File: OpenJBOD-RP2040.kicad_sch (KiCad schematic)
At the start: 61 parts, among them J1 ATX-24, J2 Bus_PCI_Express_x1, J3 Conn_02x02_Counter_Clockwise, J4 UART, J5 USB_C_Receptacle_USB2.0_16P, J9 TEMP1, Q1 MMBT3904, Q2 MMBT3904, SW1 TC-6615-6-260G, SW2 TC-6615-6-260G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

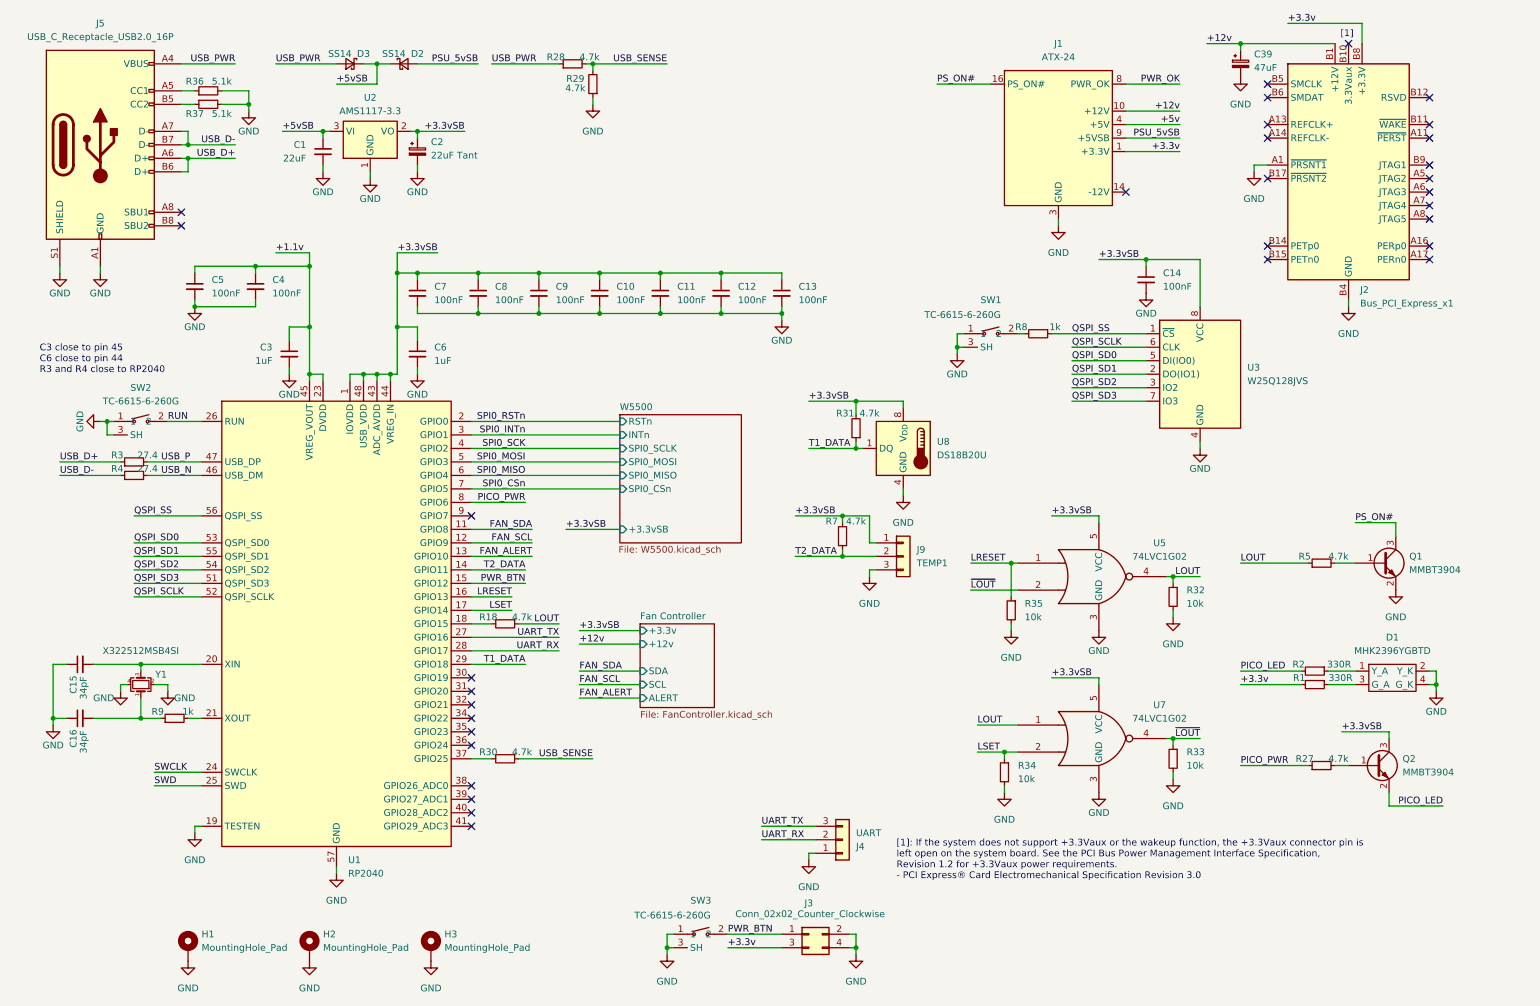
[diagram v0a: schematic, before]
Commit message: sch/pcb: SR latch caps
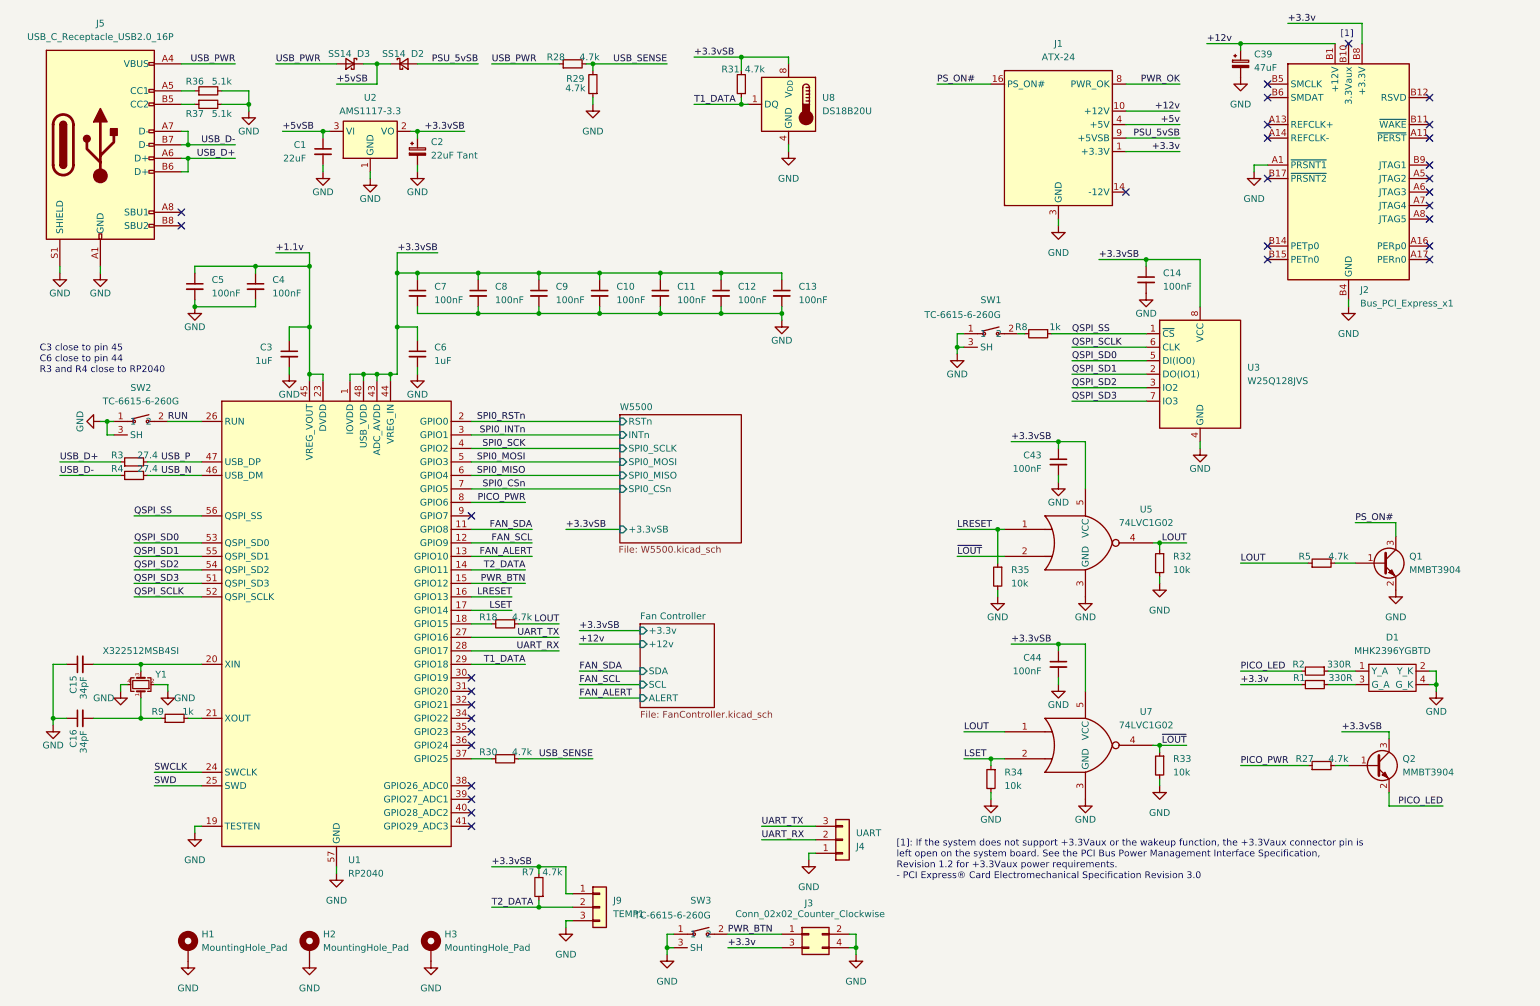
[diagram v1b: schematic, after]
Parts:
- added C43, C44: 100nF, Capacitor_SMD:C_0402_1005Metric, symbol Device:C_Small
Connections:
- net +3.3vSB: now also C43.1, C44.1
- net GND: now also C43.2, C44.2
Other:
- moved on the sheet: J9, R31, R32, R33, R34, R35, R7, U5, U7, U8

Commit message: schematic cleanup
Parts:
- removed C1: 22uF, Capacitor_SMD:C_1206_3216Metric, symbol Device:C_Small
- removed C10, C11, C12, C13, C14, C4, C43, C44, C5, C7, C8, C9: 100nF, Capacitor_SMD:C_0402_1005Metric, symbol Device:C_Small
- removed C15, C16: 34pF, Capacitor_SMD:C_0603_1608Metric, symbol Device:C_Small
- removed C2: 22uF Tant, Capacitor_Tantalum_SMD:CP_EIA-3216-18_Kemet-A, symbol Device:C_Polarized_Small
- removed C3, C6: 1uF, Capacitor_SMD:C_0402_1005Metric, symbol Device:C_Small
- removed D2, D3: SS14, Diode_SMD:D_SMA, symbol Device:D_Schottky_Small
- removed J1: ATX-24, OpenJBOD_Library:CONN-TH_M4202V-2X12P, symbol Connector:ATX-24
- removed J5: USB_C_Receptacle_USB2.0_16P, OpenJBOD_Library:USB-C-SMD_TYPE-C16PIN, symbol Connector:USB_C_Receptacle_USB2.0_16P
- removed J9: TEMP1, Connector_PinHeader_2.54mm:PinHeader_1x03_P2.54mm_Vertical, symbol Connector_Generic:Conn_01x03
- removed Q1: MMBT3904, Package_TO_SOT_SMD:SOT-23, symbol Transistor_BJT:MMBT3904
- removed R18, R28, R29, R30, R31, R5, R7: 4.7k, Resistor_SMD:R_0402_1005Metric, symbol Device:R_Small
- removed R3, R4: 27.4, Resistor_SMD:R_0402_1005Metric, symbol Device:R_Small
- removed R32, R33, R34, R35: 10k, Capacitor_SMD:C_0402_1005Metric, symbol Device:R_Small
- removed R36, R37: 5.1k, Capacitor_SMD:C_0402_1005Metric, symbol Device:R_Small
- removed R8, R9: 1k, Resistor_SMD:R_0402_1005Metric, symbol Device:R_Small
- removed SW1, SW2: TC-6615-6-260G, OpenJBOD_Library:KEY-TH_TC-6615-6-160G, symbol OpenJBOD:TC-6615-6-260G
- removed U1: RP2040, Package_DFN_QFN:QFN-56-1EP_7x7mm_P0.4mm_EP3.2x3.2mm, symbol MCU_RaspberryPi:RP2040
- removed U2: AMS1117-3.3, Package_TO_SOT_SMD:SOT-223-3_TabPin2, symbol Regulator_Linear:AMS1117-3.3
- removed U3: W25Q128JVS, Package_SO:SOIC-8_5.23x5.23mm_P1.27mm, symbol Memory_Flash:W25Q128JVS
- removed U5, U7: 74LVC1G02, Package_TO_SOT_SMD:SOT-353_SC-70-5, symbol 74xGxx:74LVC1G02
- removed U8: DS18B20U, Package_SO:MSOP-8_3x3mm_P0.65mm, symbol Sensor_Temperature:DS18B20U
- removed Y1: X322512MSB4SI, Crystal:Crystal_SMD_3225-4Pin_3.2x2.5mm, symbol Device:Crystal_GND24_Small
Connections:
- no-connect marks 32 -> 18
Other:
- sheet Fan Controller renamed Environment
- added sheet MCU (MCU.kicad_sch)
- added sheet Power (Power.kicad_sch)
- sheet Environment: file FanController.kicad_sch -> Environment.kicad_sch
- sheet Environment ports: added T1_DATA, T2_DATA; removed none
- note added: "EMC2301 DS18B20"
- note added: "Front Panel IO"
- note added: "LED Indicators"
- note added: "Mounting Holes"
- note added: "PCIe x1 Header"
- note added: "RP2040 QSPI Flash GPIO BOOTSEL switch RESET switch"
- note added: "UART"
- note added: "USB-C 24p ATX SR Latch USB Sensing 3.3v Standby"
- note added: "W5500 RJ45 NIC"
- note removed: "C3 close to pin 45 C6 close to pin 44 R3 and R4 close to RP2040"
- moved on the sheet: C39, D1, H1, H2, H3, J2, J3, J4, Q2, R1, R2, R27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

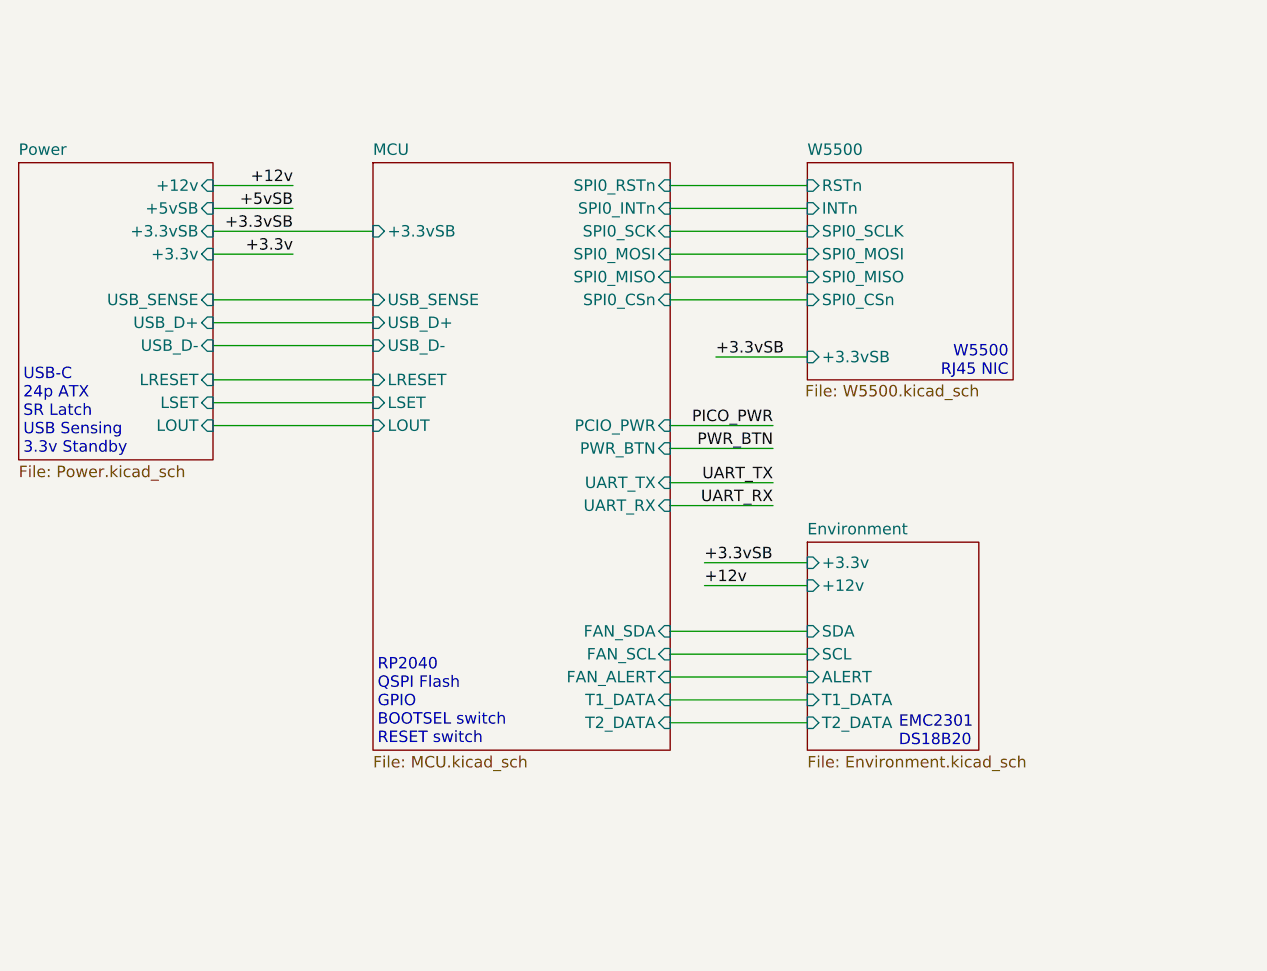
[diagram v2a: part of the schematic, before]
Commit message: rev5
Added MACROM (specific ROM holding MAC address and (optionally) board
revision)
Added more circuitry to protect the EMC2301, allowing for use with fans
with internal pull-ups.
Added USB-C
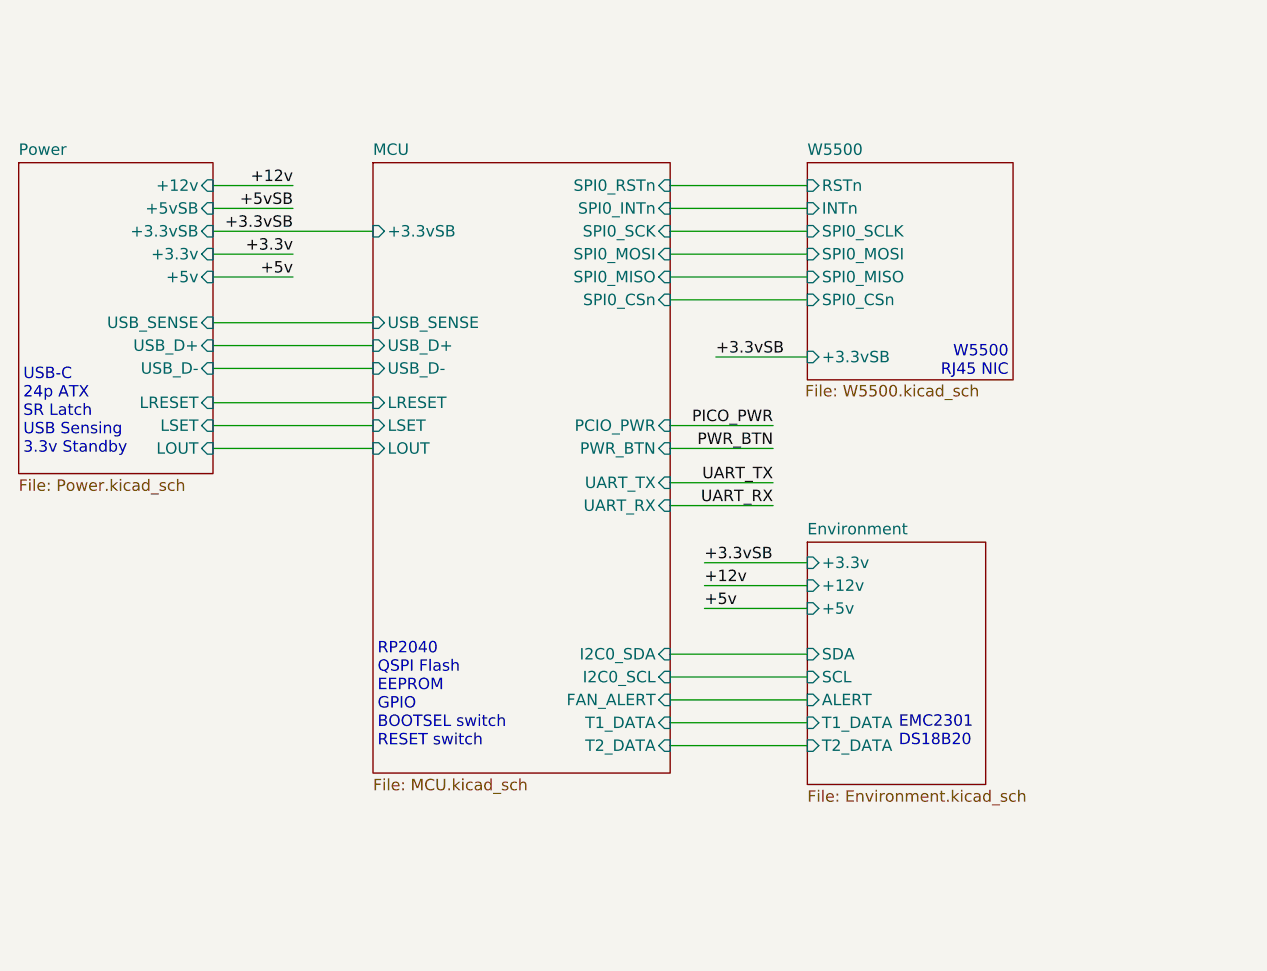
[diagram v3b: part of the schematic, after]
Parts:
- C39: JLCPCB_PN C2836440 -> (none); LCSC Part # (none) -> C2836440
- D1: JLCPCB_PN C2764899 -> (none); LCSC Part # (none) -> C2764899
- J2: JLCPCB_PN C5210918 -> (none); LCSC Part # (none) -> C5210918
- J3: JLCPCB_PN C492419 -> (none); LCSC Part # (none) -> C492419
- J4: JLCPCB_PN C2894945 -> (none); LCSC Part # (none) -> C2894945
- Q2: JLCPCB_PN C20526 -> (none); LCSC Part # (none) -> C20526
- R1, R2: JLCPCB_PN C25104 -> (none); LCSC Part # (none) -> C25104
- R27: JLCPCB_PN C25900 -> (none); LCSC Part # (none) -> C25900
- SW3: JLCPCB_PN C2845272 -> (none); LCSC Part # (none) -> C2845272
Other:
- sheet Environment ports: added +5v; removed none
- sheet MCU ports: added I2C0_SCL, I2C0_SDA; removed FAN_SCL, FAN_SDA
- sheet Power ports: added +5v; removed none
- note added: "RP2040 QSPI Flash EEPROM GPIO BOOTSEL switch RESET switch"
- note removed: "RP2040 QSPI Flash GPIO BOOTSEL switch RESET switch"
